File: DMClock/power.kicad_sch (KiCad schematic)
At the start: 23 parts, among them IC1 MP2338GTL-Z, J1 Barrel_Jack_Switch, J2 (12v LiPo battery), J3 Conn_01x02, J4 Conn_01x03, SW2 SW_SPDT

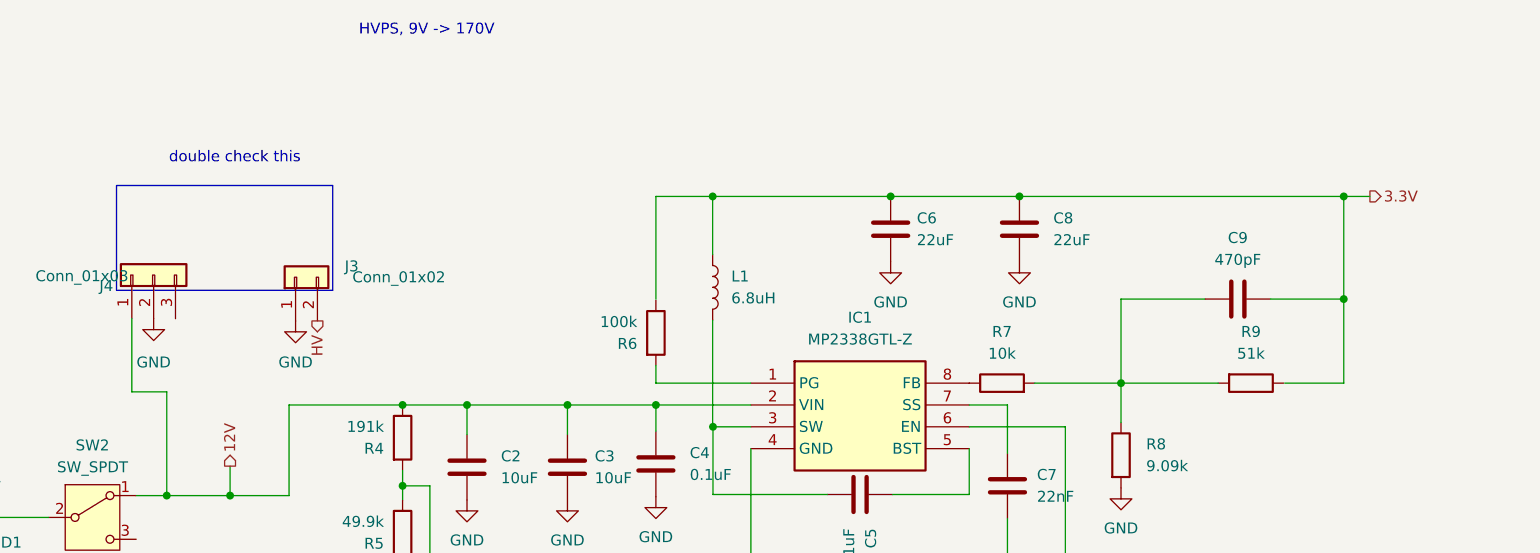
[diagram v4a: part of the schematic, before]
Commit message: finished second layer. need to finalize both first and second (double checking everything looks right, double check pwm pins, add ground plane, and finally send to pcbway. im kinda slow but hopefully done with first version pcb by tomorrow.
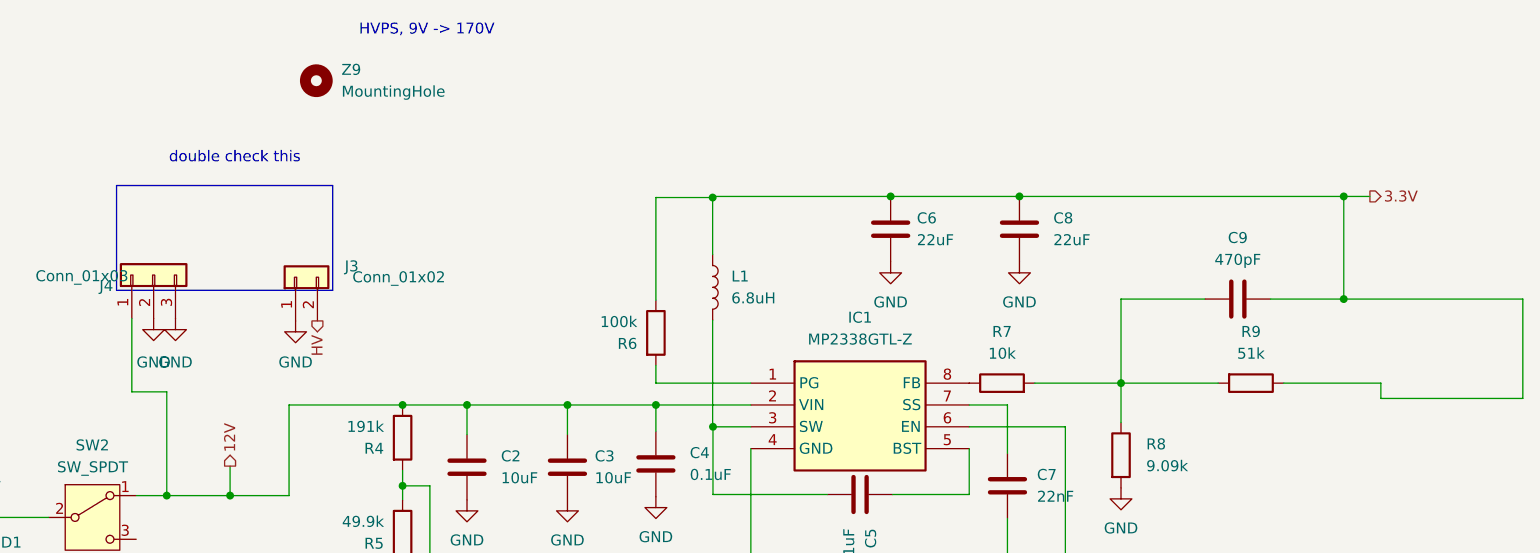
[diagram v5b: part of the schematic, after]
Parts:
- added Z9: MountingHole, MountingHole:MountingHole_2.2mm_M2, symbol Mechanical:MountingHole
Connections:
- net 3.3V: now also R6.1, R9.1
- net GND: now also J4.3 (Pin_3)
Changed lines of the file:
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@@
   (junction (at 164.846 119.5642) (diameter 0) (color 0 0 0 0)
   )
+  (junction (at 233.807 84.582) (diameter 0) (color 0 0 0 0)
+  )
   (junction (at 160.4363 99.441) (diameter 0) (color 0 0 0 0)
   )
   (junction (at 74.676 109.982) (diameter 0) (color 0 0 0 0)
   )
+  (junction (at 160.401 72.771) (diameter 0) (color 0 0 0 0)
+  )
   (junction (at 196.088 72.644) (diameter 0) (color 0 0 0 0)
   )
   (junction (at 143.51 96.901) (diameter 0) (color 0 0 0 0)
   )
-  (junction (at 160.401 72.644) (diameter 0) (color 0 0 0 0)
-  )
   (junction (at 96.901 107.442) (diameter 0) (color 0 0 0 0)
   )
@@
   (junction (at 207.899 94.361) (diameter 0) (color 0 0 0 0)
   )
-  (junction (at 233.807 84.582) (diameter 0) (color 0 0 0 0)
-  )
   (wire (pts (xy 160.4363 99.441) (xy 160.401 99.441))
     (stroke (width 0) (type default))
@@
     (stroke (width 0) (type default))
   )
-  (wire (pts (xy 153.797 72.644) (xy 160.401 72.644))
+  (wire (pts (xy 153.797 72.771) (xy 160.401 72.771))
     (stroke (width 0) (type default))
   )
@@
     (stroke (width 0) (type default))
   )
+  (wire (pts (xy 254.635 84.582) (xy 233.807 84.582))
+    (stroke (width 0) (type default))
+  )
   (wire (pts (xy 207.899 94.361) (xy 207.899 84.582))
     (stroke (width 0) (type default))
@@
     (stroke (width 0) (type default))
   )
-  (wire (pts (xy 153.797 84.582) (xy 153.797 72.644))
+  (wire (pts (xy 153.797 84.709) (xy 153.797 72.771))
     (stroke (width 0) (type default))
   )
@@
     (stroke (width 0) (type default))
   )
-  (wire (pts (xy 160.401 79.4114) (xy 160.401 72.644))
-    (stroke (width 0) (type default))
-  )
-  (wire (pts (xy 233.807 84.582) (xy 233.807 94.361))
+  (wire (pts (xy 160.401 79.4114) (xy 160.401 72.771))
+    (stroke (width 0) (type default))
+  )
+  (wire (pts (xy 254.635 84.582) (xy 254.635 96.139))
     (stroke (width 0) (type default))
   )
@@
     (stroke (width 0) (type default))
   )
+  (wire (pts (xy 238.125 94.361) (xy 226.822 94.361))
+    (stroke (width 0) (type default))
+  )
   (wire (pts (xy 197.866 94.361) (xy 207.899 94.361))
     (stroke (width 0) (type default))
@@
     (stroke (width 0) (type default))
   )
-  (wire (pts (xy 226.949 94.361) (xy 233.807 94.361))
+  (wire (pts (xy 238.125 96.139) (xy 254.635 96.139))
     (stroke (width 0) (type default))
   )
@@
     (stroke (width 0) (type default))
   )
+  (wire (pts (xy 238.125 96.139) (xy 238.125 94.361))
+    (stroke (width 0) (type default))
+  )
   (wire (pts (xy 181.102 72.644) (xy 196.088 72.644))
     (stroke (width 0) (type default))
@@
   )
   (wire (pts (xy 65.532 116.332) (xy 68.834 116.332))
+    (stroke (width 0) (type default))
+  )
+  (wire (pts (xy 160.401 72.771) (xy 160.401 72.644))
     (stroke (width 0) (type default))
   )
@@
     )
   )
+  (symbol (lib_id "power:GND") (at 97.917 86.868 0) (unit 1)
+    (in_bom yes) (on_board yes) (dnp no) (fields_autoplaced)
+    (property "Reference" "#PWR09" (at 97.917 93.218 0)
+      (effects (font (size 1.27 1.27)) hide)
+    )
+    (property "Value" "GND" (at 97.917 91.948 0)
+      (effects (font (size 1.27 1.27)))
+    )
+    (property "Footprint" "" (at 97.917 86.868 0)
+      (effects (font (size 1.27 1.27)) hide)
+    )
+    (property "Datasheet" "" (at 97.917 86.868 0)
+      (effects (font (size 1.27 1.27)) hide)
+    )
+    (pin "1")
+    (instances
+      (project "DMClock"
+        (path "/b42b345f-a3f2-4eff-9109-2f4619119d33/e2b2635d-0e87-4f37-9170-e83d5f5e5877"
+          (reference "#PWR09") (unit 1)
+        )
+      )
+    )
+  )
   (symbol (lib_id "Device:R") (at 223.012 94.361 270) (unit 1)
     (in_bom yes) (on_board yes) (dnp no) (fields_autoplaced)
@@
         )
       )
+    )
+  )
+  (symbol (lib_id "Mechanical:MountingHole") (at 114.3 59.182 0) (unit 1)
+    (in_bom yes) (on_board yes) (dnp no)
+    (property "Reference" "Z9" (at 117.221 57.912 0)
+      (effects (font (size 1.27 1.27)) (justify left))
+    )
+    (property "Value" "MountingHole" (at 117.221 60.452 0)
+      (effects (font (size 1.27 1.27)) (justify left))
+    )
+    (property "Footprint" "MountingHole:MountingHole_2.2mm_M2" (at 114.3 59.182 0)
+      (effects (font (size 1.27 1.27)) hide)
+    )
+    (property "Datasheet" "~" (at 114.3 59.182 0)
+      (effects (font (size 1.27 1.27)) hide)
+    )
+    (instances
+      (project "DMClock"
+        (path "/b42b345f-a3f2-4eff-9109-2f4619119d33/e2b2635d-0e87-4f37-9170-e83d5f5e5877"
+          (reference "Z9") (unit 1)
+        )
+      )

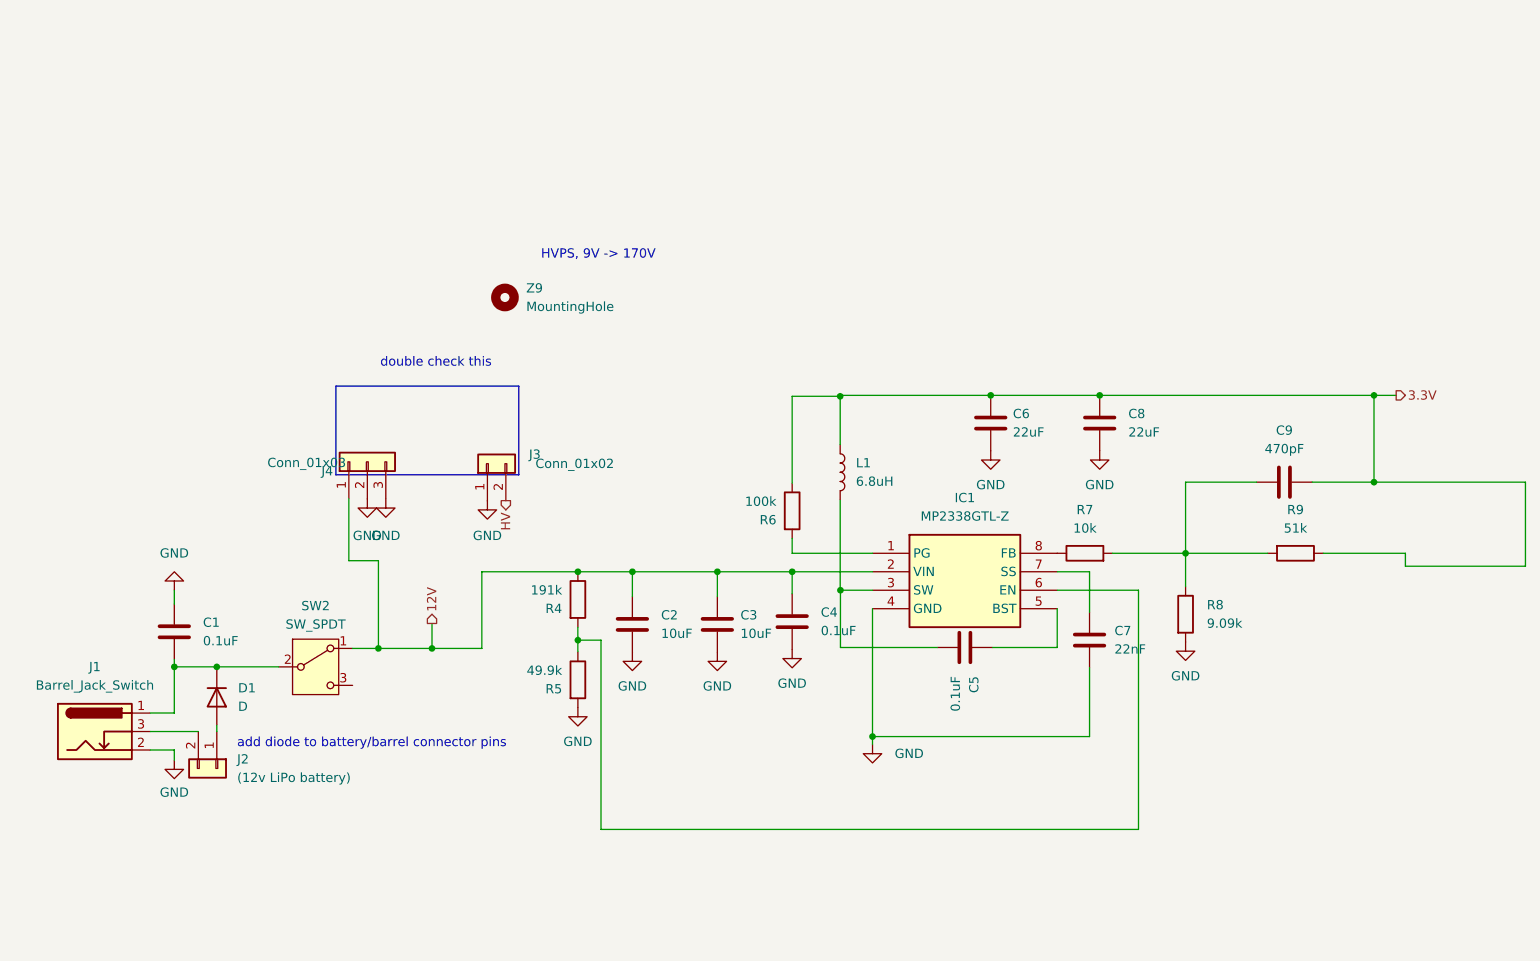
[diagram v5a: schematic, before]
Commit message: updated buck converter
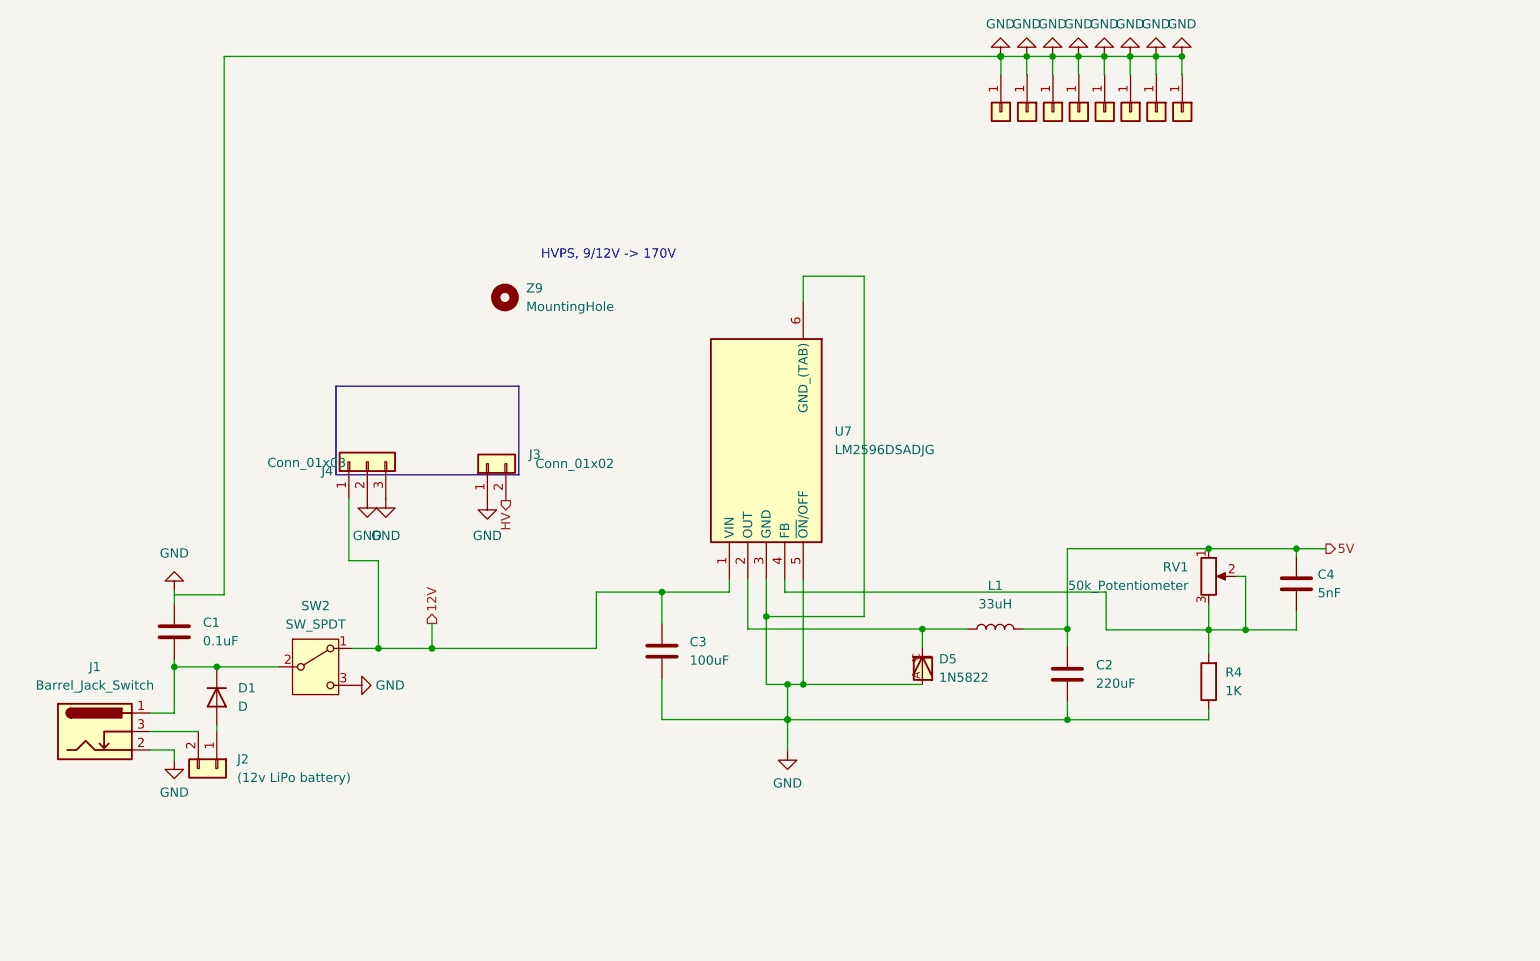
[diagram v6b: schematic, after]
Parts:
- removed C5: 0.1uF, Capacitor_SMD:C_0805_2012Metric, symbol Device:C
- removed C6, C8: 22uF, Capacitor_SMD:C_0805_2012Metric, symbol Device:C
- removed C7: 22nF, Capacitor_SMD:C_0805_2012Metric, symbol Device:C
- removed C9: 470pF, Capacitor_SMD:C_0805_2012Metric, symbol Device:C
- removed IC1: MP2338GTL-Z, Footprints:MP2338GTLZ, symbol MP2338GTL-Z:MP2338GTL-Z
- removed R5: 49.9k, Resistor_THT:R_Axial_DIN0204_L3.6mm_D1.6mm_P2.54mm_Vertical, symbol Device:R
- removed R6: 100k, Resistor_THT:R_Axial_DIN0204_L3.6mm_D1.6mm_P2.54mm_Vertical, symbol Device:R
- removed R7: 10k, Resistor_THT:R_Axial_DIN0204_L3.6mm_D1.6mm_P2.54mm_Vertical, symbol Device:R
- removed R8: 9.09k, Resistor_THT:R_Axial_DIN0204_L3.6mm_D1.6mm_P2.54mm_Vertical, symbol Device:R
- removed R9: 51k, Resistor_THT:R_Axial_DIN0204_L3.6mm_D1.6mm_P2.54mm_Vertical, symbol Device:R
- added D5: 1N5822, Footprints:DIOAD2120W130L950D530P, symbol 1N5822:1N5822
- added J10, J11, J12, J13, J14, J7, J8, J9: Conn_01x01, Connector_PinHeader_2.54mm:PinHeader_1x01_P2.54mm_Vertical, symbol Connector_Generic:Conn_01x01
- added RV1: 50k_Potentiometer, Footprints:TRIM_3306F-1-503, symbol Device:R_Potentiometer
- added U7: LM2596DSADJG, Footprints:NCP5663DSADJR4G, symbol LM2596DSADJG:LM2596DSADJG
- C2: value 10uF -> 220uF; footprint Capacitor_SMD:C_0805_2012Metric -> Footprints:WCAP-ATG8_6.3X11_DXL_
- C3: value 10uF -> 100uF; footprint Capacitor_SMD:C_0805_2012Metric -> Footprints:CAPPRD350W60D825H1300
- C4: value 0.1uF -> 5nF
- L1: value 6.8uH -> 33uH; footprint Inductor_SMD:L_0805_2012Metric -> Footprints:DO5040H333MLD
- R4: value 191k -> 1K
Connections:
- net 12V: now also C3.2, U7.1 (VIN); no longer C2.1, C3.1, C4.2, R4.1
- net GND: now also C2.1, C3.1, R4.1, SW2.3 (C), D5.A, J10.1 (Pin_1), J11.1 (Pin_1), J12.1 (Pin_1), J13.1 (Pin_1), J14.1 (Pin_1), J7.1 (Pin_1), J8.1 (Pin_1), J9.1 (Pin_1), U7.3 (GND), U7.5 (~{ON}/OFF), U7.6 (GND_(TAB)); no longer C2.2, C3.2, C4.1
- net 5V: now reaches L1.2
- net 5V: now also C2.2, C4.2, RV1.1
- net at R4.2: now also C4.1, RV1.2, RV1.3, U7.4 (FB)
- net 3.3V: no longer names the net of L1.1
- net 3.3V: now also D5.C, U7.2 (OUT)
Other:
- note added: "HVPS, 9/12V -> 170V"
- note removed: "HVPS, 9V -> 170V"
- note removed: "add diode to battery/barrel connector pins"
- note removed: "double check this"
